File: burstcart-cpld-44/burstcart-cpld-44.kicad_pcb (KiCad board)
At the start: 2 copper layers, 56 x 91 mm, 16 parts, among them J1 IEC, J2 IEC, J3 AMS1117, J4 JTAG, U1 27C512, U2 XC9572XL-VQ44, U3 AMS1117-3.3

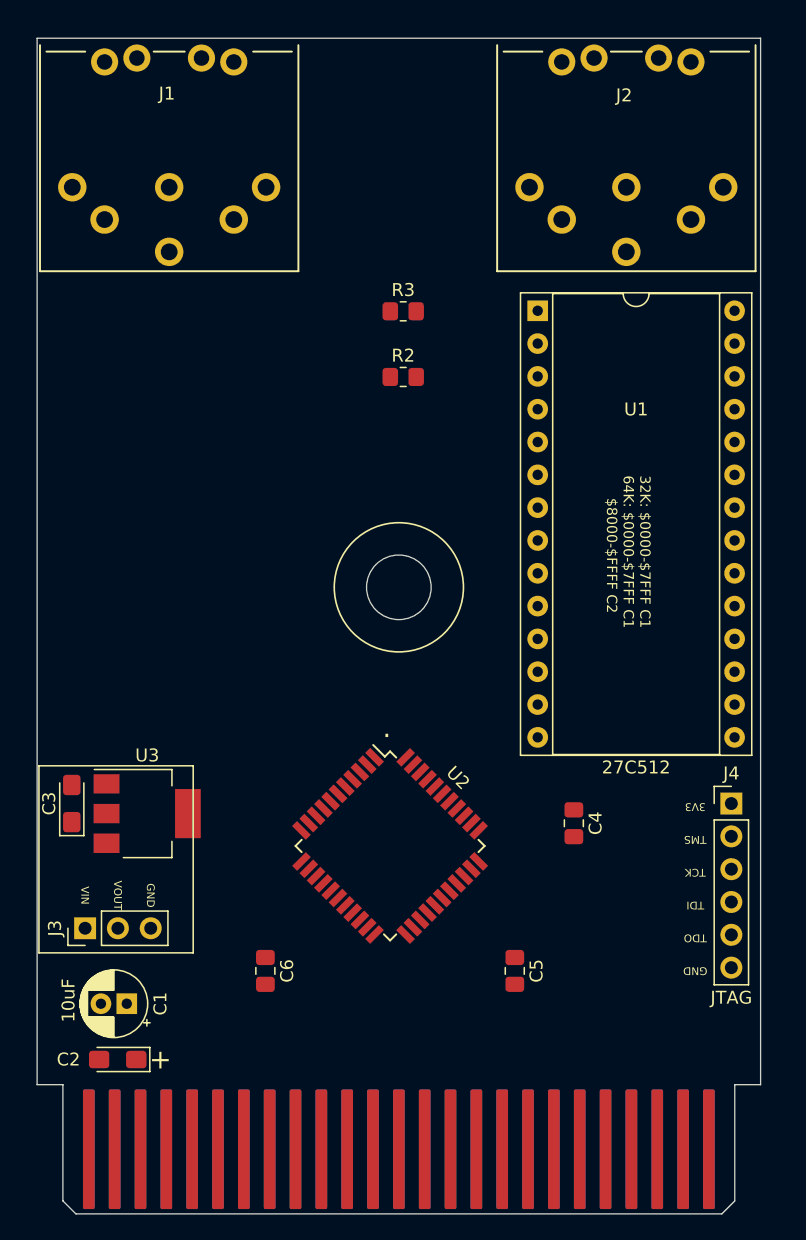
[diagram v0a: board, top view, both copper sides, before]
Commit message: finalized CPLD (VQ44) board
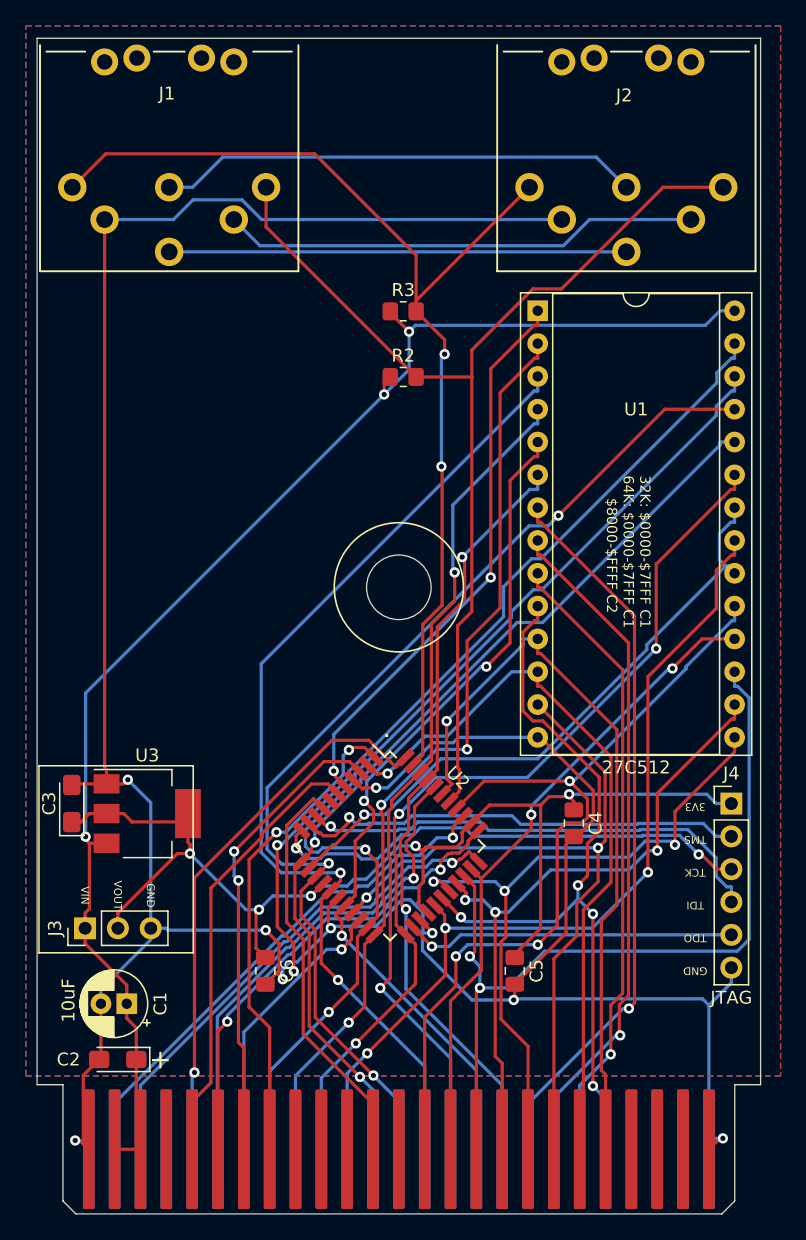
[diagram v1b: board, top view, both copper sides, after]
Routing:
- net GND: track 0.00 -> 237.8 mm, vias 0 -> 9
- net VCC: track 0.00 -> 108.6 mm, vias 0 -> 3
- net +3V3: track 0.00 -> 94.5 mm, vias 0 -> 5
- net /A14: track 0.00 -> 87.4 mm, vias 0 -> 3
- net IEC_SRQ: track 0.00 -> 84.7 mm, vias 0 -> 2
- net /A8: track 0.00 -> 84.5 mm, vias 0 -> 3
- net IEC_DATA: track 0.00 -> 84.2 mm
- net /A13: track 0.00 -> 82.7 mm, vias 0 -> 2
- net /A7: track 0.00 -> 78.0 mm, vias 0 -> 2
- net /A9: track 0.00 -> 73.2 mm, vias 0 -> 2
- net /A12: track 0.00 -> 71.9 mm, vias 0 -> 3
- net /A11: track 0.00 -> 71.1 mm, vias 0 -> 3
- net /A10: track 0.00 -> 68.4 mm, vias 0 -> 3
- net /D7: track 0.00 -> 66.9 mm, vias 0 -> 3
- net /A5: track 0.00 -> 66.8 mm, vias 0 -> 3
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- added copper zone on B.Cu, net GND
- added copper zone on F.Cu, net GND
